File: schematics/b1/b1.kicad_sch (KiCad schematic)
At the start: 37 parts, among them SW1 PWR_SW, U1 L7805, U2 AMS1117-3.3

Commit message: Assigned some footprints.
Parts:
- C1, C2, C6, C7: footprint (none) -> Capacitor_THT:CP_Radial_D4.0mm_P2.00mm
- C10, C11, C12, C13, C3, C4, C5, C8, C9: footprint (none) -> Capacitor_THT:CP_Radial_D8.0mm_P3.80mm
- JP1, JP2: footprint (none) -> Jumper:SolderJumper-2_P1.3mm_Open_TrianglePad1.0x1.5mm
- SW1: footprint (none) -> custom:SW_SPDT
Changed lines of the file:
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@@
       (effects (font (size 1.27 1.27)) (justify left))
     )
-    (property "Footprint" "" (at 87.3252 48.26 0)
+    (property "Footprint" "Capacitor_THT:CP_Radial_D8.0mm_P3.80mm" (at 87.3252 48.26 0)
       (effects (font (size 1.27 1.27)) hide)
     )
@@
       (effects (font (size 1.27 1.27)) (justify left))
     )
-    (property "Footprint" "" (at 74.6252 109.22 0)
+    (property "Footprint" "Capacitor_THT:CP_Radial_D8.0mm_P3.80mm" (at 74.6252 109.22 0)
       (effects (font (size 1.27 1.27)) hide)
     )
@@
       (effects (font (size 1.27 1.27)) (justify left))
     )
-    (property "Footprint" "" (at 60.6552 78.74 0)
+    (property "Footprint" "Capacitor_THT:CP_Radial_D4.0mm_P2.00mm" (at 60.6552 78.74 0)
       (effects (font (size 1.27 1.27)) hide)
     )
@@
       (effects (font (size 1.27 1.27)) (justify left))
     )
-    (property "Footprint" "" (at 100.0252 78.74 0)
+    (property "Footprint" "Capacitor_THT:CP_Radial_D8.0mm_P3.80mm" (at 100.0252 78.74 0)
       (effects (font (size 1.27 1.27)) hide)
     )
@@
       (effects (font (size 1.27 1.27)) (justify left))
     )
-    (property "Footprint" "" (at 74.6252 48.26 0)
+    (property "Footprint" "Capacitor_THT:CP_Radial_D8.0mm_P3.80mm" (at 74.6252 48.26 0)
       (effects (font (size 1.27 1.27)) hide)
     )
@@
       (effects (font (size 1.27 1.27)) (justify left))
     )
-    (property "Footprint" "" (at 74.6252 78.74 0)
+    (property "Footprint" "Capacitor_THT:CP_Radial_D8.0mm_P3.80mm" (at 74.6252 78.74 0)
       (effects (font (size 1.27 1.27)) hide)
     )
@@
       (effects (font (size 1.27 1.27)) hide)
     )
-    (property "Footprint" "" (at 148.59 90.17 0)
+    (property "Footprint" "Jumper:SolderJumper-2_P1.3mm_Open_TrianglePad1.0x1.5mm" (at 148.59 90.17 0)
       (effects (font (size 1.27 1.27)) hide)
     )
@@
       (effects (font (size 1.27 1.27)) (justify left))
     )
-    (property "Footprint" "" (at 25.4 29.21 0)
+    (property "Footprint" "custom:SW_SPDT" (at 25.4 29.21 0)
       (effects (font (size 1.27 1.27)) hide)
     )
@@
       (effects (font (size 1.27 1.27)) (justify left))
     )
-    (property "Footprint" "" (at 100.0252 48.26 0)
+    (property "Footprint" "Capacitor_THT:CP_Radial_D8.0mm_P3.80mm" (at 100.0252 48.26 0)
       (effects (font (size 1.27 1.27)) hide)
     )
@@
       (effects (font (size 1.27 1.27)) (justify left))
     )
-    (property "Footprint" "" (at 87.3252 109.22 0)
+    (property "Footprint" "Capacitor_THT:CP_Radial_D8.0mm_P3.80mm" (at 87.3252 109.22 0)
       (effects (font (size 1.27 1.27)) hide)
     )
@@
       (effects (font (size 1.27 1.27)) hide)
     )
-    (property "Footprint" "" (at 148.59 72.39 0)
+    (property "Footprint" "Jumper:SolderJumper-2_P1.3mm_Open_TrianglePad1.0x1.5mm" (at 148.59 72.39 0)
       (effects (font (size 1.27 1.27)) hide)
     )
@@
       (effects (font (size 1.27 1.27)) (justify left))
     )
-    (property "Footprint" "" (at 87.3252 78.74 0)
+    (property "Footprint" "Capacitor_THT:CP_Radial_D8.0mm_P3.80mm" (at 87.3252 78.74 0)
       (effects (font (size 1.27 1.27)) hide)
     )
@@
       (effects (font (size 1.27 1.27)) (justify left))
     )
-    (property "Footprint" "" (at 60.6552 48.26 0)
+    (property "Footprint" "Capacitor_THT:CP_Radial_D4.0mm_P2.00mm" (at 60.6552 48.26 0)
       (effects (font (size 1.27 1.27)) hide)
     )
@@
       (effects (font (size 1.27 1.27)) (justify left))
     )
-    (property "Footprint" "" (at 100.0252 109.22 0)
+    (property "Footprint" "Capacitor_THT:CP_Radial_D8.0mm_P3.80mm" (at 100.0252 109.22 0)
       (effects (font (size 1.27 1.27)) hide)
     )
@@
       (effects (font (size 1.27 1.27)) (justify right))
     )
-    (property "Footprint" "" (at 40.3352 78.74 0)
+    (property "Footprint" "Capacitor_THT:CP_Radial_D4.0mm_P2.00mm" (at 40.3352 78.74 0)
       (effects (font (size 1.27 1.27)) hide)
     )
@@
       (effects (font (size 1.27 1.27)) (justify right))
     )
-    (property "Footprint" "" (at 40.3352 48.26 0)
-      (effects (font (size 1.27 1.27)) hide)
-    )
+    (property "Footprint" "Capacitor_THT:CP_Radial_D4.0mm_P2.00mm" (at 40.3352 48.26 0)
+      (effects (font (size 1.27 1.27)) hide)
+    )

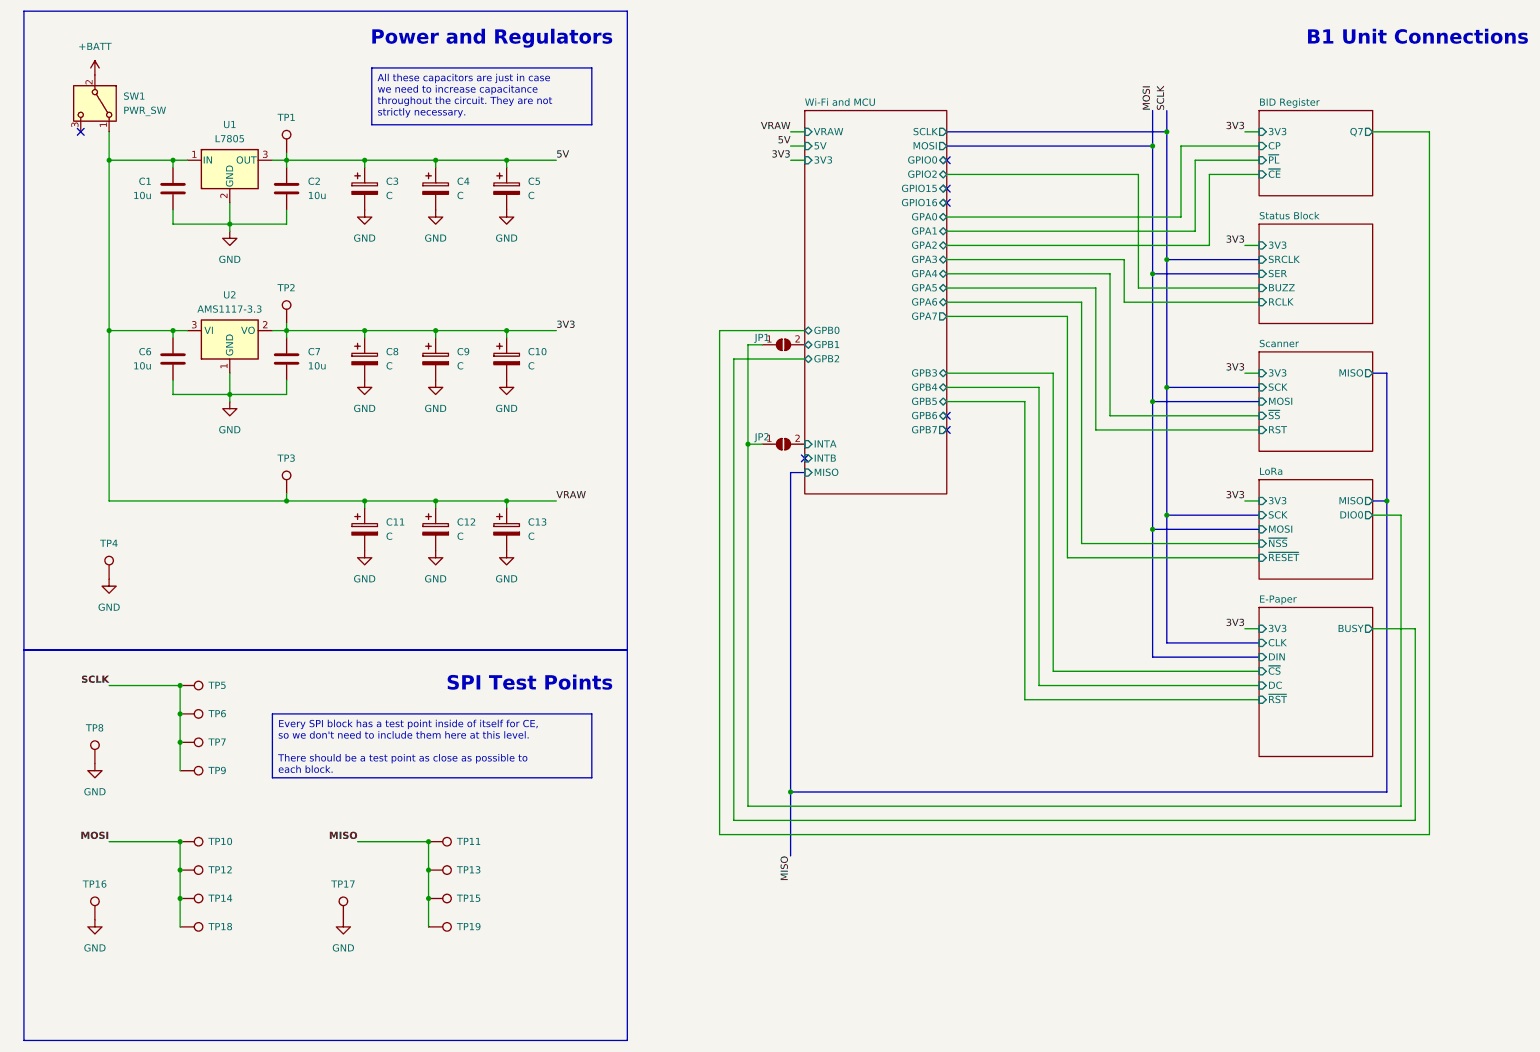
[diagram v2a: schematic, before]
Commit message: Resolved all ERC messages.
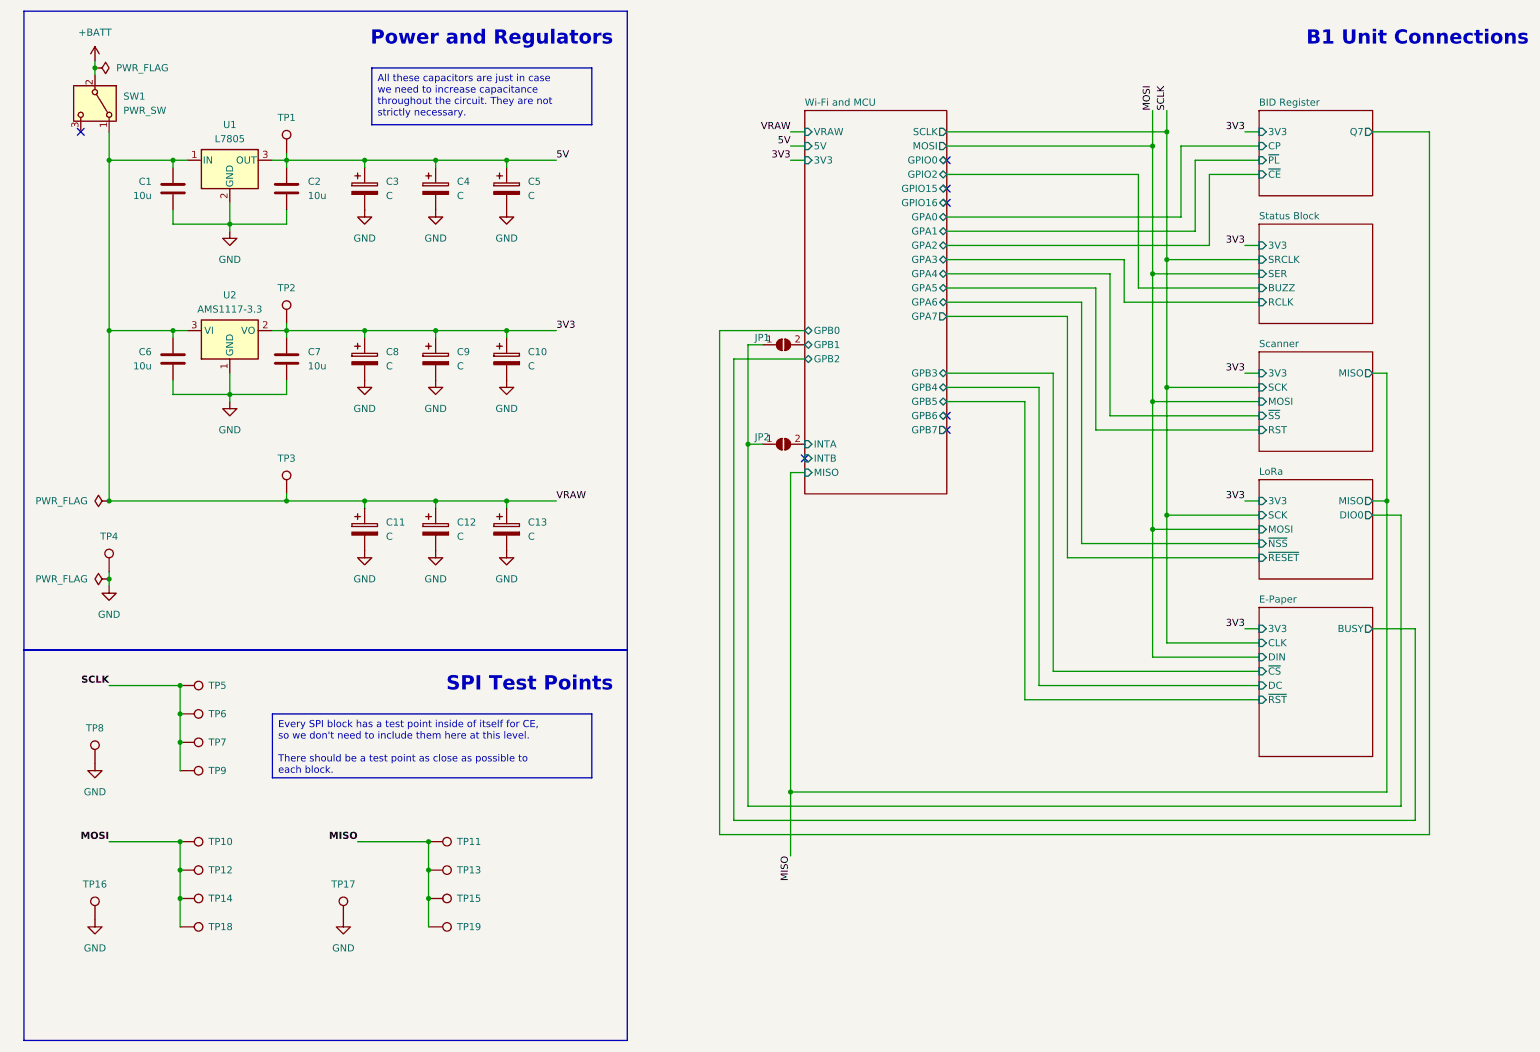
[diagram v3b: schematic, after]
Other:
- moved on the sheet: TP4

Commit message: Finished assigning footprints.
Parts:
- TP1, TP10, TP11, TP12, TP13, TP14, TP15, TP16, TP17, TP18, TP19, TP2, TP3, TP4, TP5, TP6, TP7, TP8, TP9: footprint (none) -> TestPoint:TestPoint_Loop_D2.50mm_Drill1.0mm
- U1: footprint (none) -> Package_TO_SOT_THT:TO-220-3_Horizontal_TabDown
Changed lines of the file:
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@@
       (effects (font (size 1.27 1.27)) (justify left) hide)
     )
-    (property "Footprint" "" (at 64.77 68.58 0)
+    (property "Footprint" "TestPoint:TestPoint_Loop_D2.50mm_Drill1.0mm" (at 64.77 68.58 0)
       (effects (font (size 1.27 1.27)) hide)
     )
@@
       (effects (font (size 1.27 1.27)) (justify left) hide)
     )
-    (property "Footprint" "" (at 40.64 153.67 0)
+    (property "Footprint" "TestPoint:TestPoint_Loop_D2.50mm_Drill1.0mm" (at 40.64 153.67 0)
       (effects (font (size 1.27 1.27)) hide)
     )
@@
       (effects (font (size 1.27 1.27)) (justify left) hide)
     )
-    (property "Footprint" "" (at 30.48 147.32 0)
+    (property "Footprint" "TestPoint:TestPoint_Loop_D2.50mm_Drill1.0mm" (at 30.48 147.32 0)
       (effects (font (size 1.27 1.27)) hide)
     )
@@
       (effects (font (size 1.27 1.27)) (justify left) hide)
     )
-    (property "Footprint" "" (at 74.93 175.26 0)
+    (property "Footprint" "TestPoint:TestPoint_Loop_D2.50mm_Drill1.0mm" (at 74.93 175.26 0)
       (effects (font (size 1.27 1.27)) hide)
     )
@@
       (effects (font (size 1.27 1.27)) (justify left) hide)
     )
-    (property "Footprint" "" (at 85.09 181.61 0)
+    (property "Footprint" "TestPoint:TestPoint_Loop_D2.50mm_Drill1.0mm" (at 85.09 181.61 0)
       (effects (font (size 1.27 1.27)) hide)
     )
@@
       (effects (font (size 1.27 1.27)) (justify left) hide)
     )
-    (property "Footprint" "" (at 64.77 38.1 0)
+    (property "Footprint" "TestPoint:TestPoint_Loop_D2.50mm_Drill1.0mm" (at 64.77 38.1 0)
       (effects (font (size 1.27 1.27)) hide)
     )
@@
       (effects (font (size 1.27 1.27)) (justify left) hide)
     )
-    (property "Footprint" "" (at 85.09 176.53 0)
+    (property "Footprint" "TestPoint:TestPoint_Loop_D2.50mm_Drill1.0mm" (at 85.09 176.53 0)
       (effects (font (size 1.27 1.27)) hide)
     )
@@
       (effects (font (size 1.27 1.27)) (justify left) hide)
     )
-    (property "Footprint" "" (at 33.02 113.03 0)
+    (property "Footprint" "TestPoint:TestPoint_Loop_D2.50mm_Drill1.0mm" (at 33.02 113.03 0)
       (effects (font (size 1.27 1.27)) hide)
     )
@@
       (effects (font (size 1.27 1.27)) (justify left) hide)
     )
-    (property "Footprint" "" (at 40.64 176.53 0)
+    (property "Footprint" "TestPoint:TestPoint_Loop_D2.50mm_Drill1.0mm" (at 40.64 176.53 0)
       (effects (font (size 1.27 1.27)) hide)
     )
@@
       (effects (font (size 1.27 1.27)) (justify left) hide)
     )
-    (property "Footprint" "" (at 85.09 171.45 0)
+    (property "Footprint" "TestPoint:TestPoint_Loop_D2.50mm_Drill1.0mm" (at 85.09 171.45 0)
       (effects (font (size 1.27 1.27)) hide)
     )
@@
       (effects (font (size 1.27 1.27)) (justify left) hide)
     )
-    (property "Footprint" "" (at 40.64 166.37 0)
+    (property "Footprint" "TestPoint:TestPoint_Loop_D2.50mm_Drill1.0mm" (at 40.64 166.37 0)
       (effects (font (size 1.27 1.27)) hide)
     )
@@
       (effects (font (size 1.27 1.27)))
     )
-    (property "Footprint" "" (at 50.165 43.18 0)
+    (property "Footprint" "Package_TO_SOT_THT:TO-220-3_Horizontal_TabDown" (at 50.165 43.18 0)
       (effects (font (size 1.27 1.27) italic) (justify left) hide)
     )
@@
       (effects (font (size 1.27 1.27)) (justify left) hide)
     )
-    (property "Footprint" "" (at 64.77 99.06 0)
+    (property "Footprint" "TestPoint:TestPoint_Loop_D2.50mm_Drill1.0mm" (at 64.77 99.06 0)
       (effects (font (size 1.27 1.27)) hide)
     )
@@
       (effects (font (size 1.27 1.27)) (justify left) hide)
     )
-    (property "Footprint" "" (at 40.64 181.61 0)
+    (property "Footprint" "TestPoint:TestPoint_Loop_D2.50mm_Drill1.0mm" (at 40.64 181.61 0)
       (effects (font (size 1.27 1.27)) hide)
     )
@@
       (effects (font (size 1.27 1.27)) (justify left) hide)
     )
-    (property "Footprint" "" (at 85.09 166.37 0)
+    (property "Footprint" "TestPoint:TestPoint_Loop_D2.50mm_Drill1.0mm" (at 85.09 166.37 0)
       (effects (font (size 1.27 1.27)) hide)
     )
@@
       (effects (font (size 1.27 1.27)) (justify left) hide)
     )
-    (property "Footprint" "" (at 40.64 171.45 0)
+    (property "Footprint" "TestPoint:TestPoint_Loop_D2.50mm_Drill1.0mm" (at 40.64 171.45 0)
       (effects (font (size 1.27 1.27)) hide)
     )
@@
       (effects (font (size 1.27 1.27)) (justify left) hide)
     )
-    (property "Footprint" "" (at 40.64 148.59 0)
+    (property "Footprint" "TestPoint:TestPoint_Loop_D2.50mm_Drill1.0mm" (at 40.64 148.59 0)
       (effects (font (size 1.27 1.27)) hide)
     )
@@
       (effects (font (size 1.27 1.27)) (justify left) hide)
     )
-    (property "Footprint" "" (at 40.64 138.43 0)
+    (property "Footprint" "TestPoint:TestPoint_Loop_D2.50mm_Drill1.0mm" (at 40.64 138.43 0)
       (effects (font (size 1.27 1.27)) hide)
     )
@@
       (effects (font (size 1.27 1.27)) (justify left) hide)
     )
-    (property "Footprint" "" (at 40.64 143.51 0)
+    (property "Footprint" "TestPoint:TestPoint_Loop_D2.50mm_Drill1.0mm" (at 40.64 143.51 0)
       (effects (font (size 1.27 1.27)) hide)
     )
@@
       (effects (font (size 1.27 1.27)) (justify left) hide)
     )
-    (property "Footprint" "" (at 30.48 175.26 0)
-      (effects (font (size 1.27 1.27)) hide)
-    )
+    (property "Footprint" "TestPoint:TestPoint_Loop_D2.50mm_Drill1.0mm" (at 30.48 175.26 0)
+      (effects (font (size 1.27 1.27)) hide)
+    )
